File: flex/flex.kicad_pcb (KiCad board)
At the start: 2 copper layers, 48.8 x 41.5 mm, 20 parts, among them J1 Conn_01x06_Female, J2 Conn_01x03_Female, SW19 SW_Push, SW5 SW_Push, SW9 SW_Push

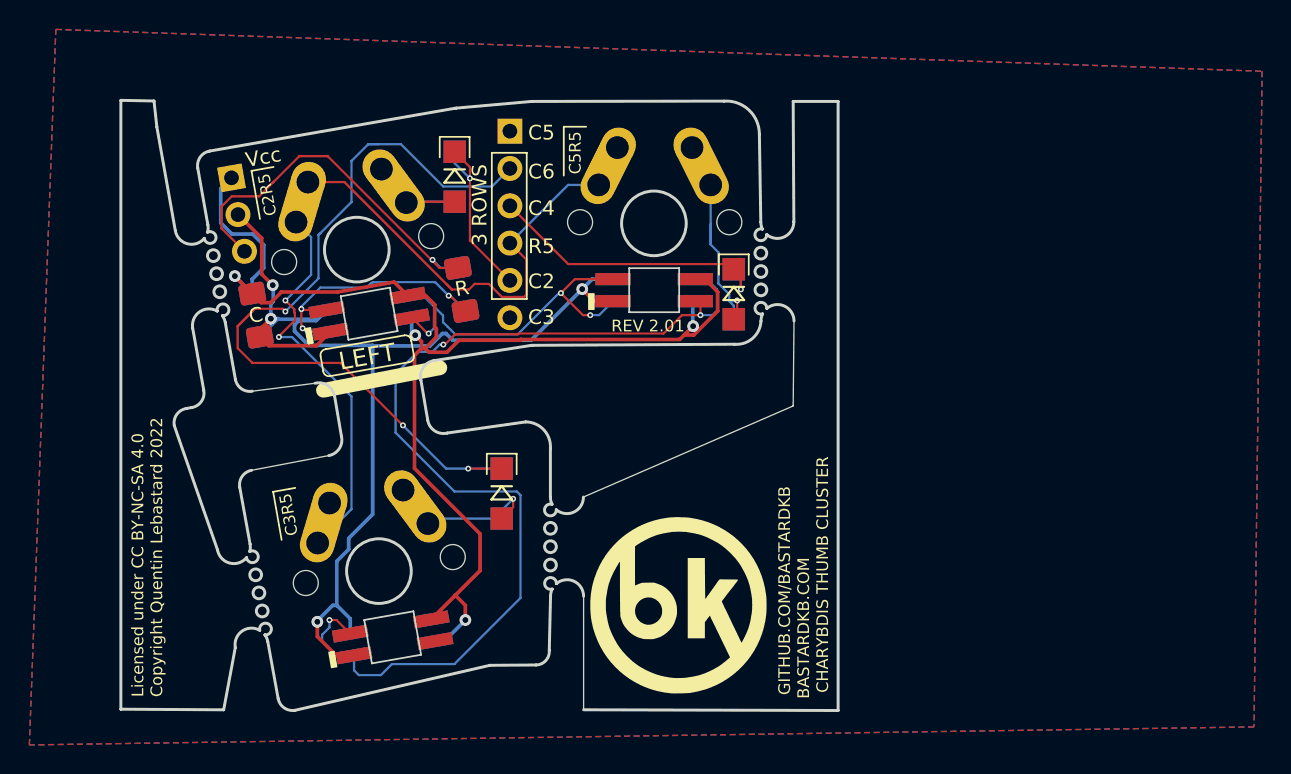
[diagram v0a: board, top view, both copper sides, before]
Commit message: ec11 button connector
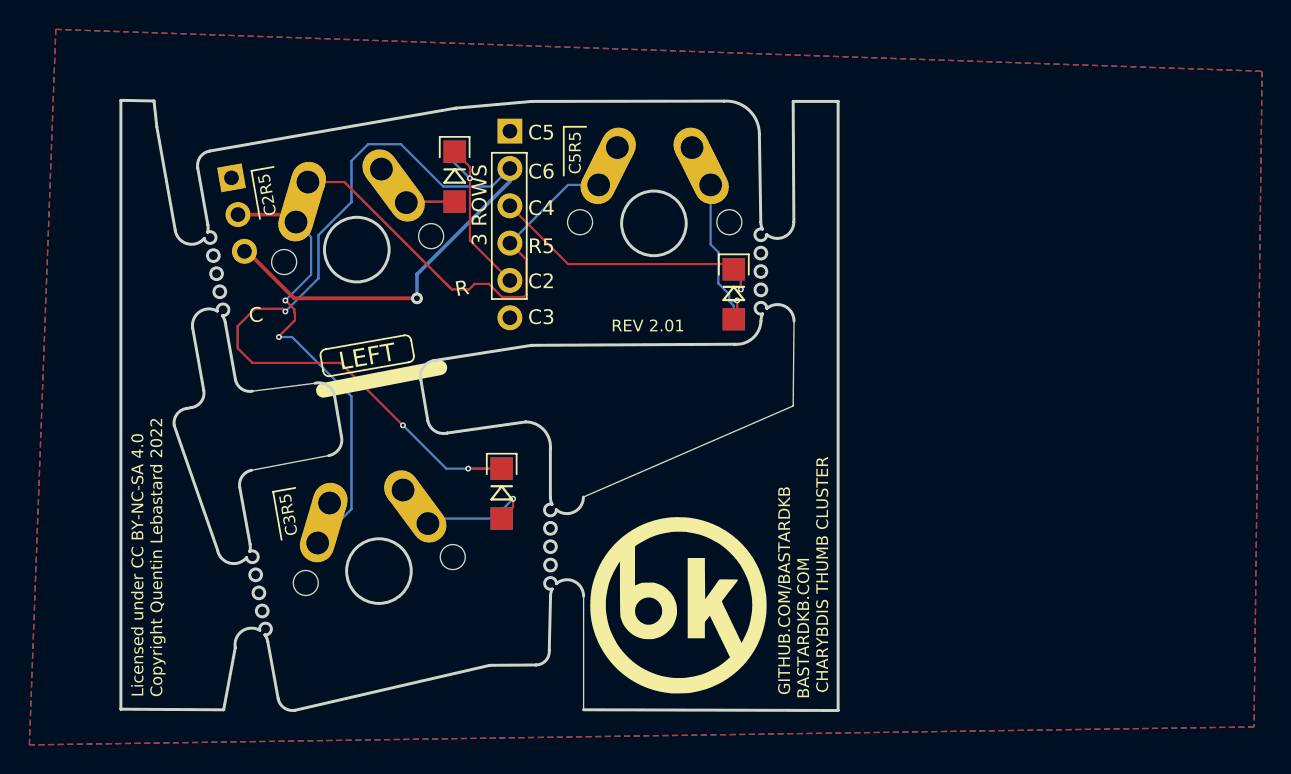
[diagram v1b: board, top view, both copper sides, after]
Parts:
- removed C1, C2: C, LED_SMD:LED_1206_3216Metric_Pad1.42x1.75mm_HandSolder
- removed D10, D12, D2: SK6812MINI, libs2:YS-SK6812MINI-E_REVERSE
- removed D11, D13, D3: SK6812MINI, libs2:YS-SK6812MINI-E_REVERSE_NO_EDGECUT
- removed R1, R2: R, Resistor_SMD:R_1206_3216Metric_Pad1.42x1.75mm_HandSolder
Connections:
- J2 pad 1: Vcc -> unconnected-(J2-Pin_1-Pad1)
- J2 pad 2: Gnd -> row1
- J2 pad 3: Din -> col6
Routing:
- net Vcc: track 87.1 -> 0.00 mm, vias 4 -> 0
- net Gnd: track 77.7 -> 0.00 mm, vias 4 -> 0
- net Net-(D10-Pad1): track 69.9 -> 0.00 mm, vias 3 -> 0
- net Net-(D12-Pad1): track 28.0 -> 0.00 mm, vias 3 -> 0
- net Din: track 26.4 -> 0.00 mm, vias 1 -> 0
- net col6: track 56.4 -> 78.6 mm, vias 3 -> 4
- net Net-(D12-Pad3): track 19.5 -> 0.00 mm, vias 3 -> 0
- net row1: track 57.9 -> 62.5 mm
- net Net-(D19-A): track 13.1 -> 11.7 mm
- added copper zone on B.Cu, net row1
- added copper zone on F.Cu, net row1
- removed copper zone on B.Cu, net Gnd
- removed copper zone on F.Cu, net Gnd
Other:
- board text added: "Row"
- board text removed: "Vcc"
